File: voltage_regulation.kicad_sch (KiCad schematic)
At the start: 69 parts, among them J1 Conn_01x07_Male, J2 Conn_01x07_Male, U10 74LS74, U13 74LS32, U14 74LS05, U17 74LS30, U2 74LS123, U3 74F04, U4 74LS221, U40 74LS20, U5 74LS08, U6 74LS32

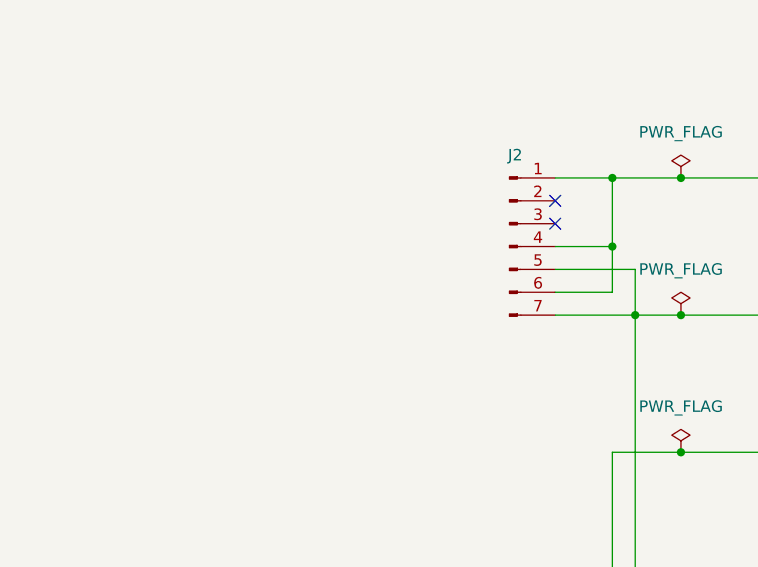
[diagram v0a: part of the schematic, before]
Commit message: Improved signal naming
clearer naming of some signals for better readability
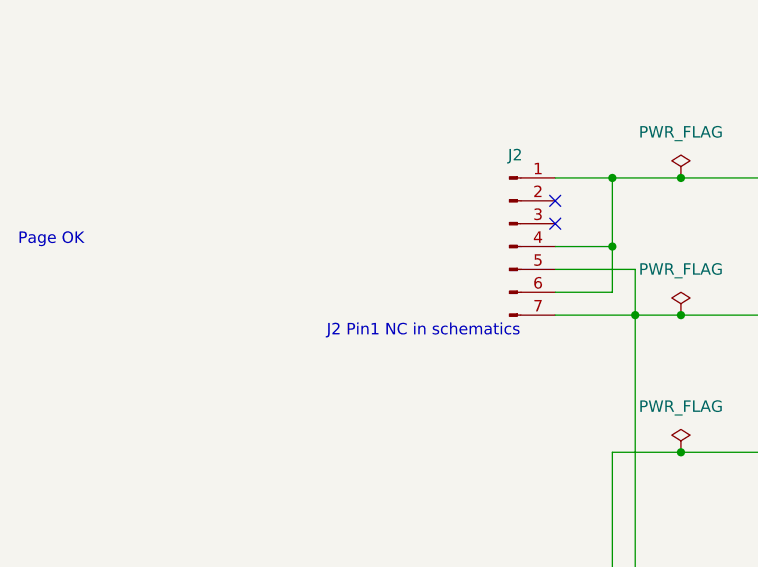
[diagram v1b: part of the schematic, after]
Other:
- note added: "J2 Pin1 NC in schematics"
- note added: "Page OK"
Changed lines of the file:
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@@
     (effects (font (size 5 5)) (justify left bottom))
+  )
+  (text "Page OK" (at 44.45 50.8 0)
+    (effects (font (size 1.27 1.27)) (justify left bottom))
   )
   (text "-5V Decoupling\n" (at 96.52 185.42 0)
@@
     (effects (font (size 5 5)) (justify left bottom))
   )
+  (text "J2 Pin1 NC in schematics" (at 78.74 60.96 0)
+    (effects (font (size 1.27 1.27)) (justify left bottom))
+  )
   (label "-5V" (at 189.23 73.66 0) (fields_autoplaced)
